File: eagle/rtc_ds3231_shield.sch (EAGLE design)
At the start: 16 parts, among them U1 ARDUINO_SHIELDLABEL

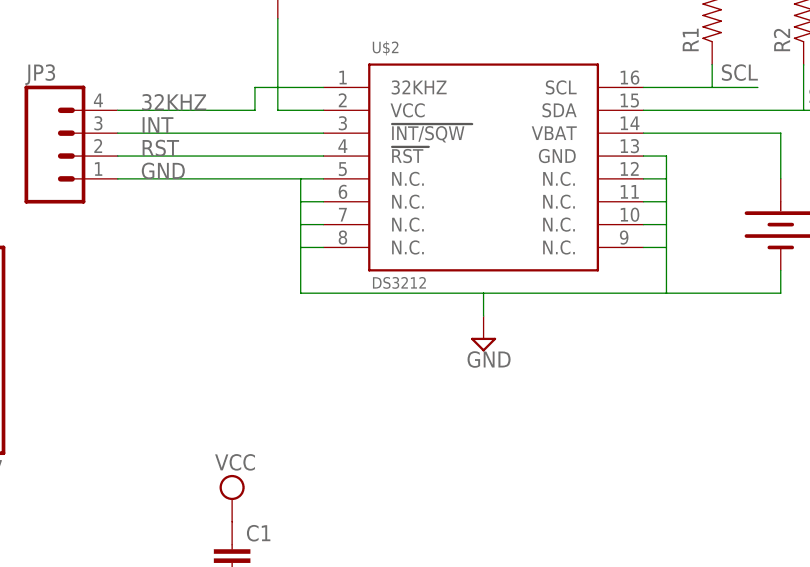
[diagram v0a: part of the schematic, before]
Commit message: 2nd Initial Commit
Typo on the RTC Chip being used.
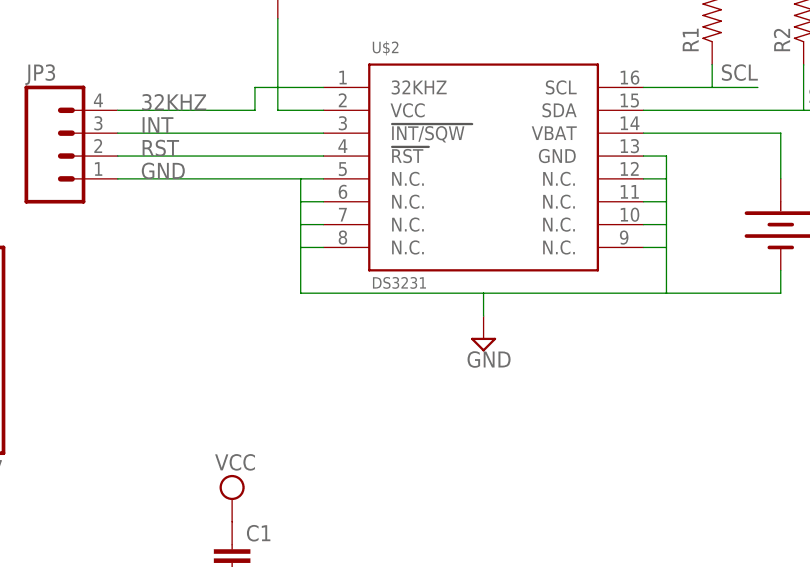
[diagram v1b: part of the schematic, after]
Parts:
- U$2: value DS3212 -> DS3231
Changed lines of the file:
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@@
 <part name="JP1" library="SparkFun" deviceset="M02" device="PTH" value="I2C_HDR"/>
 <part name="JP2" library="SparkFun" deviceset="M02" device="PTH" value="IOREF"/>
-<part name="U$2" library="Add-Ohms" deviceset="DS3231" device="" value="DS3212"/>
+<part name="U$2" library="Add-Ohms" deviceset="DS3231" device="" value="DS3231"/>
 <part name="R1" library="Add-Ohms" deviceset="RESISTOR" device="1206"/>
 <part name="R2" library="Add-Ohms" deviceset="RESISTOR" device="1206"/>

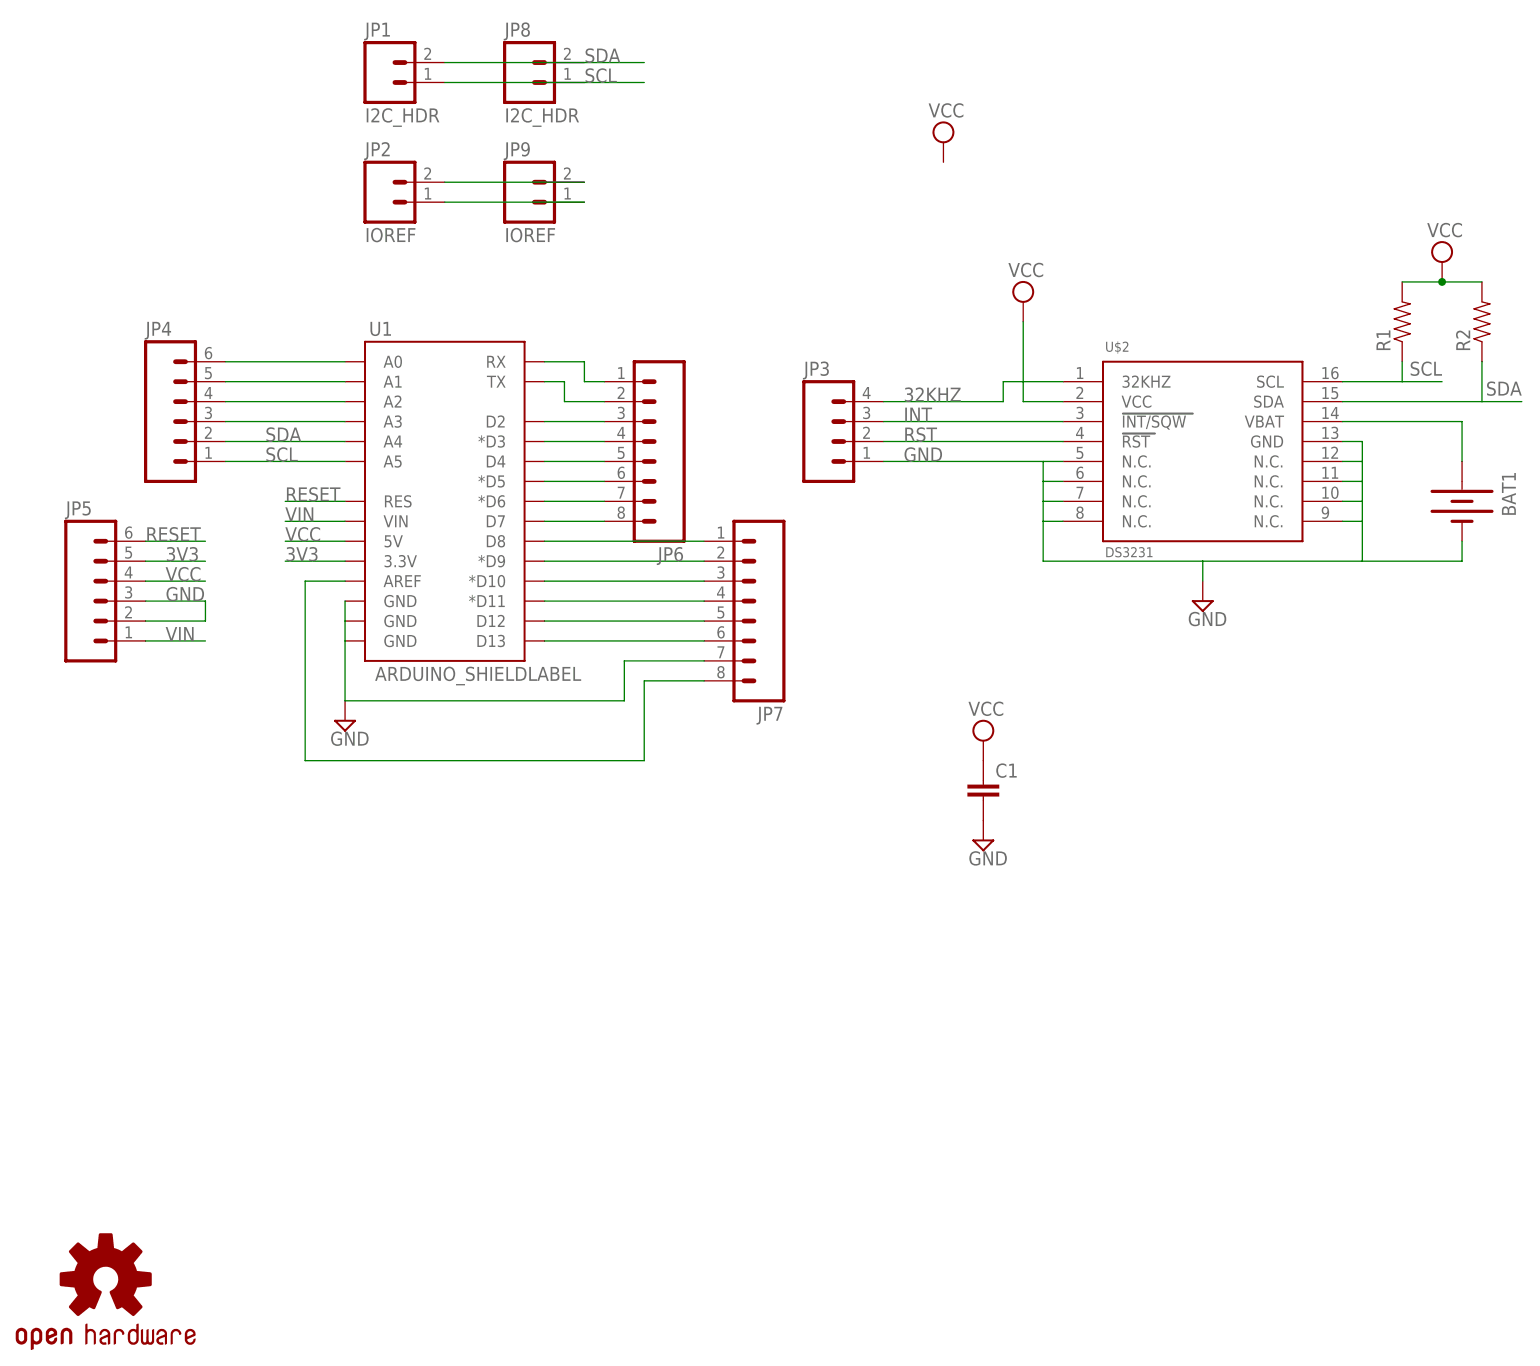
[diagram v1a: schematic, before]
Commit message: Rev1b Updates
Added LED, RESET Button, some silk screen, cleaned up silkscreen on
back, made prototyping area clean with 0.1" spacing.
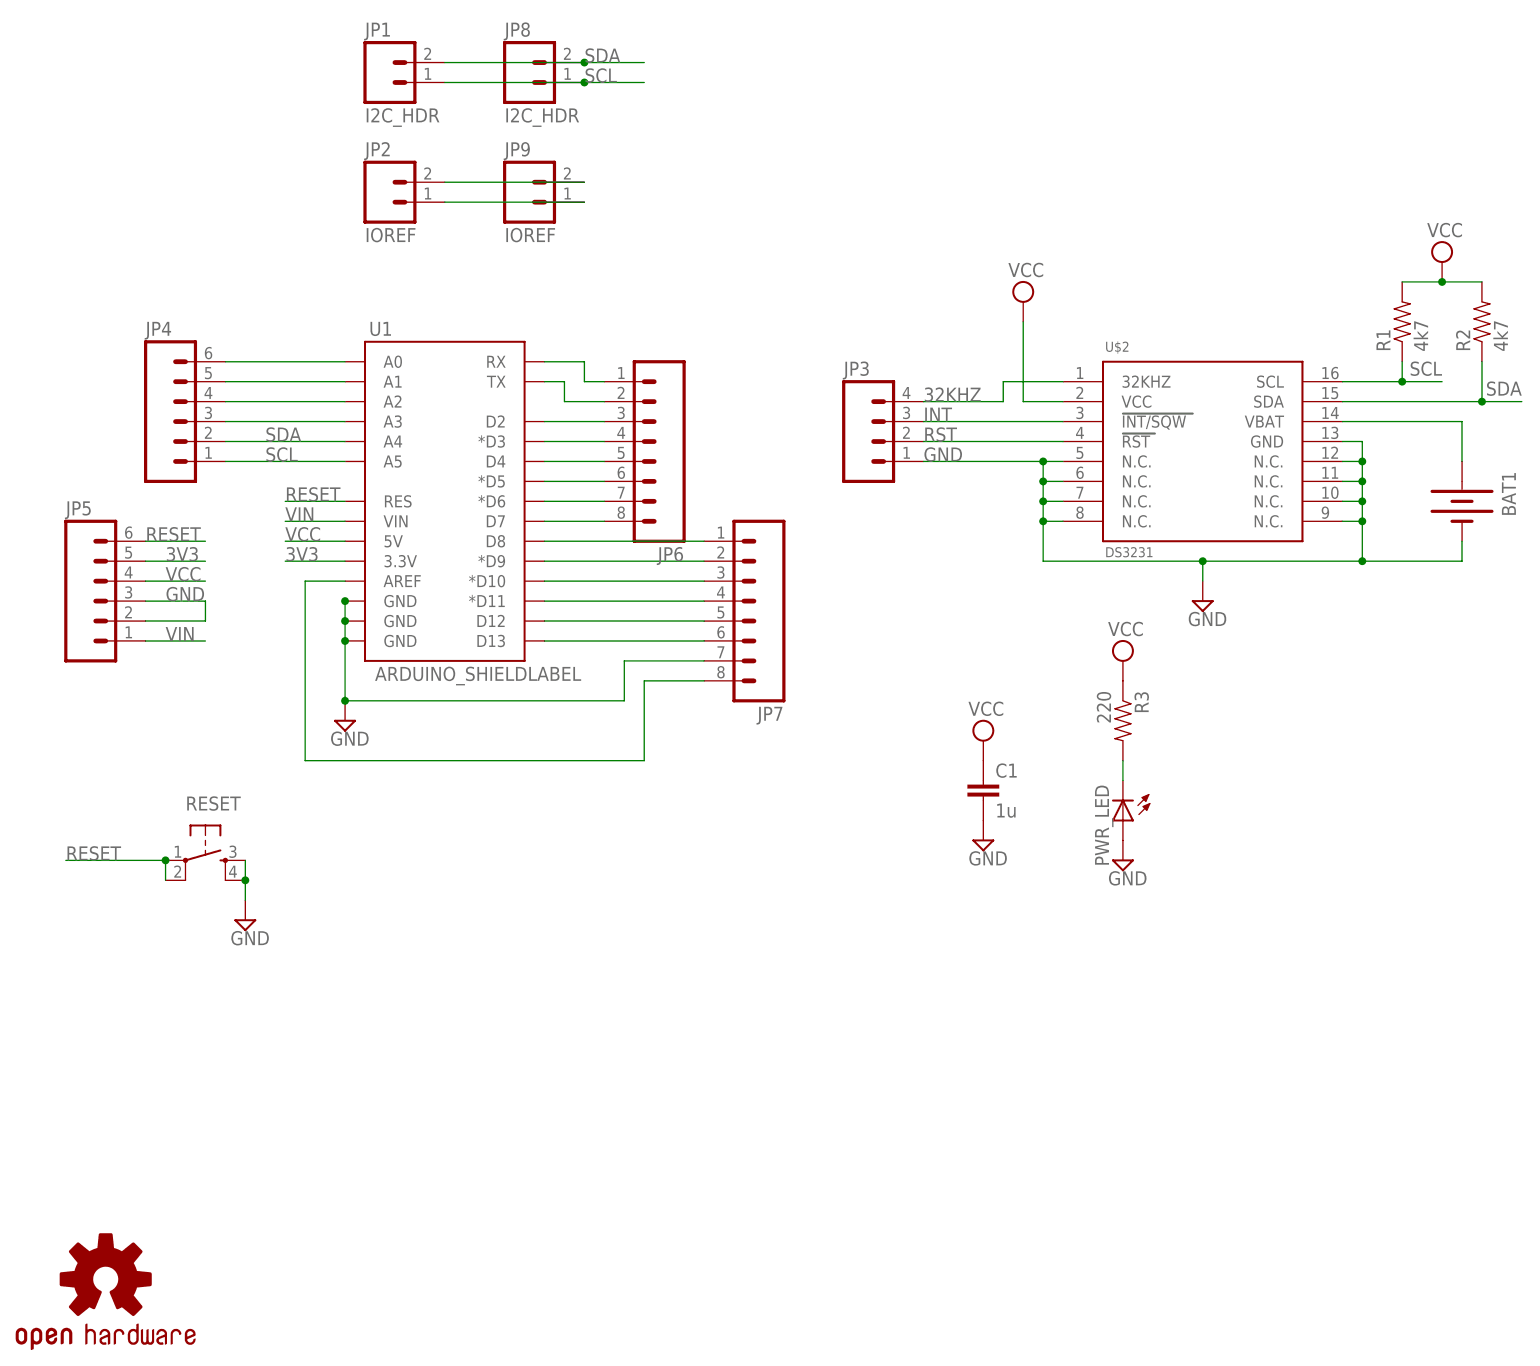
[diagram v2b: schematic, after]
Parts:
- added PWR_LED: (no value), Add-Ohms:LED1206
- added R3: 220, Add-Ohms:RESISTOR1206
- added RESET: (no value), Add-Ohms:TAC_SWITCHSMD
- C1: value (none) -> 1u
- R1, R2: value (none) -> 4k7
- renumbered U$1 to U$3
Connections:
- new net N$5: PWR_LED.C, R3.2
- net GND: now also PWR_LED.A, RESET.3, RESET.4
- net RESET: now also RESET.1, RESET.2
- net VCC: now also R3.1
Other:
- moved on the sheet: JP3
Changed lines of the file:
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@@
 <parts>
 <part name="FRAME1" library="Add-Ohms" deviceset="FRAME-LETTER" device=""/>
-<part name="U$1" library="Add-Ohms" deviceset="OSHW-LOGO" device="M"/>
+<part name="U$3" library="Add-Ohms" deviceset="OSHW-LOGO" device="M"/>
 <part name="U1" library="Add-Ohms" deviceset="ARDUINO_SHIELD" device="LABEL"/>
 <part name="JP1" library="SparkFun" deviceset="M02" device="PTH" value="I2C_HDR"/>
 <part name="JP2" library="SparkFun" deviceset="M02" device="PTH" value="IOREF"/>
 <part name="U$2" library="Add-Ohms" deviceset="DS3231" device="" value="DS3231"/>
-<part name="R1" library="Add-Ohms" deviceset="RESISTOR" device="1206"/>
-<part name="R2" library="Add-Ohms" deviceset="RESISTOR" device="1206"/>
+<part name="R1" library="Add-Ohms" deviceset="RESISTOR" device="1206" value="4k7"/>
+<part name="R2" library="Add-Ohms" deviceset="RESISTOR" device="1206" value="4k7"/>
 <part name="SUPPLY2" library="supply2" deviceset="GND" device=""/>
 <part name="BAT1" library="Add-Ohms" deviceset="BATTERY" device="12MM"/>
 <part name="SUPPLY1" library="supply2" deviceset="VCC" device=""/>
 <part name="SUPPLY3" library="supply2" deviceset="VCC" device=""/>
-<part name="SUPPLY4" library="supply2" deviceset="VCC" device=""/>
 <part name="JP3" library="SparkFun" deviceset="M04" device="PTH"/>
 <part name="JP4" library="SparkFun" deviceset="M06" device="SIP"/>
@@
 <part name="JP8" library="SparkFun" deviceset="M02" device="PTH" value="I2C_HDR"/>
 <part name="JP9" library="SparkFun" deviceset="M02" device="PTH" value="IOREF"/>
-<part name="C1" library="Add-Ohms" deviceset="CAP" device="1206"/>
+<part name="C1" library="Add-Ohms" deviceset="CAP" device="1206" value="1u"/>
 <part name="SUPPLY6" library="supply2" deviceset="VCC" device=""/>
 <part name="SUPPLY7" library="supply2" deviceset="GND" device=""/>
+<part name="RESET" library="Add-Ohms" deviceset="TAC_SWITCH" device="SMD"/>
+<part name="PWR_LED" library="Add-Ohms" deviceset="LED" device="1206"/>
+<part name="R3" library="Add-Ohms" deviceset="RESISTOR" device="1206" value="220"/>
+<part name="SUPPLY8" library="supply2" deviceset="VCC" device=""/>
+<part name="SUPPLY9" library="supply2" deviceset="GND" device=""/>
+<part name="SUPPLY10" library="supply2" deviceset="GND" device=""/>
 </parts>
 <sheets>
@@
 <instance part="FRAME1" gate="G$1" x="0" y="0"/>
 <instance part="FRAME1" gate="G$2" x="147.32" y="0"/>
-<instance part="U$1" gate="G$1" x="12.7" y="12.7"/>
+<instance part="U$3" gate="G$1" x="12.7" y="12.7"/>
 <instance part="U1" gate="G$1" x="55.88" y="111.76"/>
 <instance part="JP1" gate="G$1" x="48.26" y="165.1"/>
@@
 <instance part="SUPPLY1" gate="G$1" x="182.88" y="142.24"/>
 <instance part="SUPPLY3" gate="G$1" x="129.54" y="137.16"/>
-<instance part="SUPPLY4" gate="G$1" x="119.38" y="157.48"/>
-<instance part="JP3" gate="G$1" x="106.68" y="119.38"/>
+<instance part="JP3" gate="G$1" x="111.76" y="119.38"/>
 <instance part="JP4" gate="G$1" x="22.86" y="121.92"/>
 <instance part="JP5" gate="G$1" x="12.7" y="99.06"/>
@@
 <instance part="SUPPLY6" gate="G$1" x="124.46" y="81.28"/>
 <instance part="SUPPLY7" gate="GND" x="124.46" y="68.58"/>
+<instance part="RESET" gate="S" x="25.4" y="66.04"/>
+<instance part="PWR_LED" gate="G$1" x="142.24" y="71.12" rot="R180"/>
+<instance part="R3" gate="G$1" x="142.24" y="83.82" rot="R270"/>
+<instance part="SUPPLY8" gate="G$1" x="142.24" y="91.44"/>
+<instance part="SUPPLY9" gate="GND" x="142.24" y="66.04"/>
+<instance part="SUPPLY10" gate="GND" x="30.48" y="58.42"/>
 </instances>
 <busses>
@@
 <wire x1="185.42" y1="104.14" x2="172.72" y2="104.14" width="0.1524" layer="91"/>
 <pinref part="JP3" gate="G$1" pin="1"/>
-<wire x1="111.76" y1="116.84" x2="132.08" y2="116.84" width="0.1524" layer="91"/>
-<label x="114.3" y="116.84" size="1.778" layer="95"/>
+<wire x1="116.84" y1="116.84" x2="132.08" y2="116.84" width="0.1524" layer="91"/>
+<label x="116.84" y="116.84" size="1.778" layer="95"/>
+<junction x="172.72" y="116.84"/>
+<junction x="172.72" y="114.3"/>
+<junction x="172.72" y="111.76"/>
+<junction x="172.72" y="109.22"/>
+<junction x="132.08" y="116.84"/>
+<junction x="132.08" y="114.3"/>
+<junction x="132.08" y="111.76"/>
+<junction x="132.08" y="109.22"/>
+<junction x="172.72" y="104.14"/>
+<junction x="152.4" y="104.14"/>
 </segment>
 <segment>
@@
 <wire x1="78.74" y1="91.44" x2="78.74" y2="86.36" width="0.1524" layer="91"/>
 <wire x1="78.74" y1="86.36" x2="43.18" y2="86.36" width="0.1524" layer="91"/>
+<junction x="43.18" y="99.06"/>
+<junction x="43.18" y="96.52"/>
+<junction x="43.18" y="93.98"/>
+<junction x="43.18" y="86.36"/>
 </segment>
 <segment>
@@
 <pinref part="SUPPLY7" gate="GND" pin="GND"/>
 </segment>
+<segment>
+<pinref part="PWR_LED" gate="G$1" pin="A"/>
+<pinref part="SUPPLY9" gate="GND" pin="GND"/>
+</segment>
+<segment>
+<pinref part="RESET" gate="S" pin="3"/>
+<pinref part="RESET" gate="S" pin="4"/>
+<wire x1="30.48" y1="66.04" x2="30.48" y2="63.5" width="0.1524" layer="91"/>
+<wire x1="30.48" y1="63.5" x2="30.48" y2="60.96" width="0.1524" layer="91"/>
+<pinref part="SUPPLY10" gate="GND" pin="GND"/>
+<junction x="30.48" y="63.5"/>
+</segment>
 </net>
 <net name="SCL" class="0">
@@
 <wire x1="177.8" y1="127" x2="182.88" y2="127" width="0.1524" layer="91"/>
 <label x="182.88" y="129.54" size="1.778" layer="95" rot="R180"/>
+<junction x="177.8" y="127"/>
 </segment>
 <segment>
@@
 <wire x1="73.66" y1="165.1" x2="81.28" y2="165.1" width="0.1524" layer="91"/>
 <label x="73.66" y="165.1" size="1.778" layer="95"/>
+<junction x="73.66" y="165.1"/>
 </segment>
 </net>
@@
 <wire x1="187.96" y1="124.46" x2="193.04" y2="124.46" width="0.1524" layer="91"/>
 <label x="193.04" y="127" size="1.778" layer="95" rot="R180"/>
+<junction x="187.96" y="124.46"/>
 </segment>
 <segment>
@@
 <wire x1="73.66" y1="167.64" x2="81.28" y2="167.64" width="0.1524" layer="91"/>
 <label x="73.66" y="167.64" size="1.778" layer="95"/>
+<junction x="73.66" y="167.64"/>
 </segment>
 </net>
@@
 <pinref part="SUPPLY6" gate="G$1" pin="VCC"/>
 </segment>
+<segment>
+<pinref part="R3" gate="G$1" pin="1"/>
+<pinref part="SUPPLY8" gate="G$1" pin="VCC"/>
+</segment>
 </net>
 <net name="RST" class="0">
@@
 <pinref part="JP3" gate="G$1" pin="2"/>
 <pinref part="U$2" gate="G$1" pin="RST"/>
-<wire x1="111.76" y1="119.38" x2="134.62" y2="119.38" width="0.1524" layer="91"/>
-<label x="114.3" y="119.38" size="1.778" layer="95"/>
+<wire x1="116.84" y1="119.38" x2="134.62" y2="119.38" width="0.1524" layer="91"/>
+<label x="116.84" y="119.38" size="1.778" layer="95"/>
 </segment>
 </net>
@@
 <pinref part="JP3" gate="G$1" pin="3"/>
 <pinref part="U$2" gate="G$1" pin="INT/SQW"/>
-<wire x1="111.76" y1="121.92" x2="134.62" y2="121.92" width="0.1524" layer="91"/>
-<label x="114.3" y="121.92" size="1.778" layer="95"/>
+<wire x1="116.84" y1="121.92" x2="134.62" y2="121.92" width="0.1524" layer="91"/>
+<label x="116.84" y="121.92" size="1.778" layer="95"/>
 </segment>
 </net>
@@
 <segment>
 <pinref part="JP3" gate="G$1" pin="4"/>
-<wire x1="111.76" y1="124.46" x2="127" y2="124.46" width="0.1524" layer="91"/>
+<wire x1="116.84" y1="124.46" x2="127" y2="124.46" width="0.1524" layer="91"/>
 <wire x1="127" y1="124.46" x2="127" y2="127" width="0.1524" layer="91"/>
 <pinref part="U$2" gate="G$1" pin="32KHZ"/>
 <wire x1="127" y1="127" x2="134.62" y2="127" width="0.1524" layer="91"/>
-<label x="114.3" y="124.46" size="1.778" layer="95"/>
+<label x="116.84" y="124.46" size="1.778" layer="95"/>
 </segment>
 </net>
@@
 <label x="35.56" y="111.76" size="1.778" layer="95"/>
 </segment>
+<segment>
+<pinref part="RESET" gate="S" pin="2"/>
+<pinref part="RESET" gate="S" pin="1"/>
+<wire x1="20.32" y1="63.5" x2="20.32" y2="66.04" width="0.1524" layer="91"/>
+<wire x1="20.32" y1="66.04" x2="7.62" y2="66.04" width="0.1524" layer="91"/>
+<label x="7.62" y="66.04" size="1.778" layer="95"/>
+<junction x="20.32" y="66.04"/>
+</segment>
 </net>
 <net name="3V3" class="0">
@@
 </segment>
 </net>
+<net name="N$5" class="0">
+<segment>
+<pinref part="R3" gate="G$1" pin="2"/>
+<pinref part="PWR_LED" gate="G$1" pin="C"/>
+<wire x1="142.24" y1="78.74" x2="142.24" y2="76.2" width="0.1524" layer="91"/>
+</segment>
+</net>
 </nets>
 </sheet>
 </sheets>
+<errors>
+</errors>
 </schematic>
 </drawing>
